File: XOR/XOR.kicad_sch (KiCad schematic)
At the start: 9 parts, among them J1 AudioJack2_SwitchT, J2 AudioJack2_SwitchT, J3 AudioJack2_SwitchT, Q1 BSS84, Q2 BSS84, Q3 BSS84, Q4 BSS84, Q5 BSS84, Q6 BSS84

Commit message: Layout XOR
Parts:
- J1, J2, J3: footprint (none) -> Custom_FP:PJ398SM

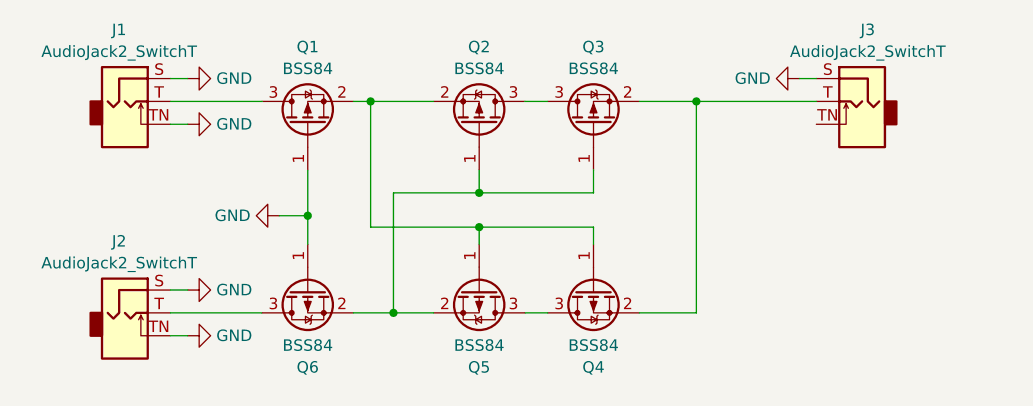
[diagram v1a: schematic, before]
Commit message: Add pulldown when XOR inputs are high
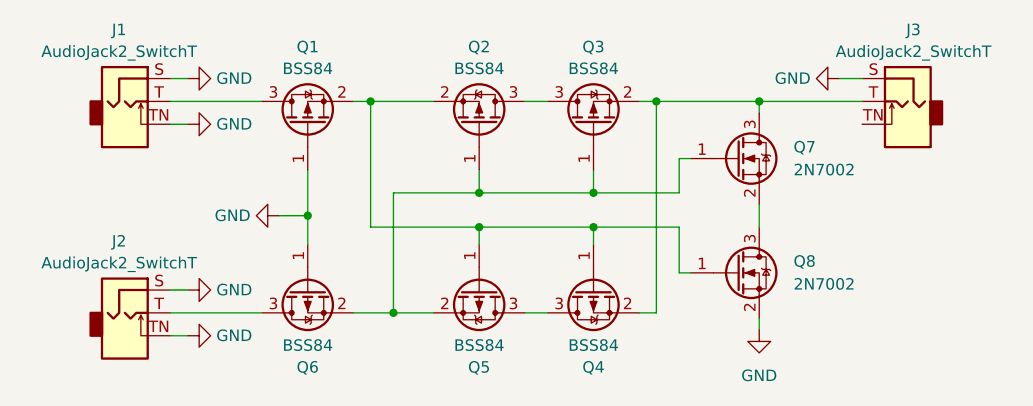
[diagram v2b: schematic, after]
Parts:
- added Q7, Q8: 2N7002, Package_TO_SOT_SMD:SOT-23, symbol Transistor_FET:2N7002
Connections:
- net GND: now also Q8.2 (S)
- net at Q2.1 (G), Q3.1 (G), Q5.2 (S)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: now also Q7.1 (G)
- net at J3.T, Q3.2 (S), Q4.2 (S): now also Q7.3 (D)
- net at Q1.2 (S), Q2.2 (S), Q4.1 (G)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: now also Q8.1 (G)
- new net: Q7.2 (S), Q8.3 (D)
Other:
- moved on the sheet: J3
